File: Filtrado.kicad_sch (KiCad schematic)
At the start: 31 parts

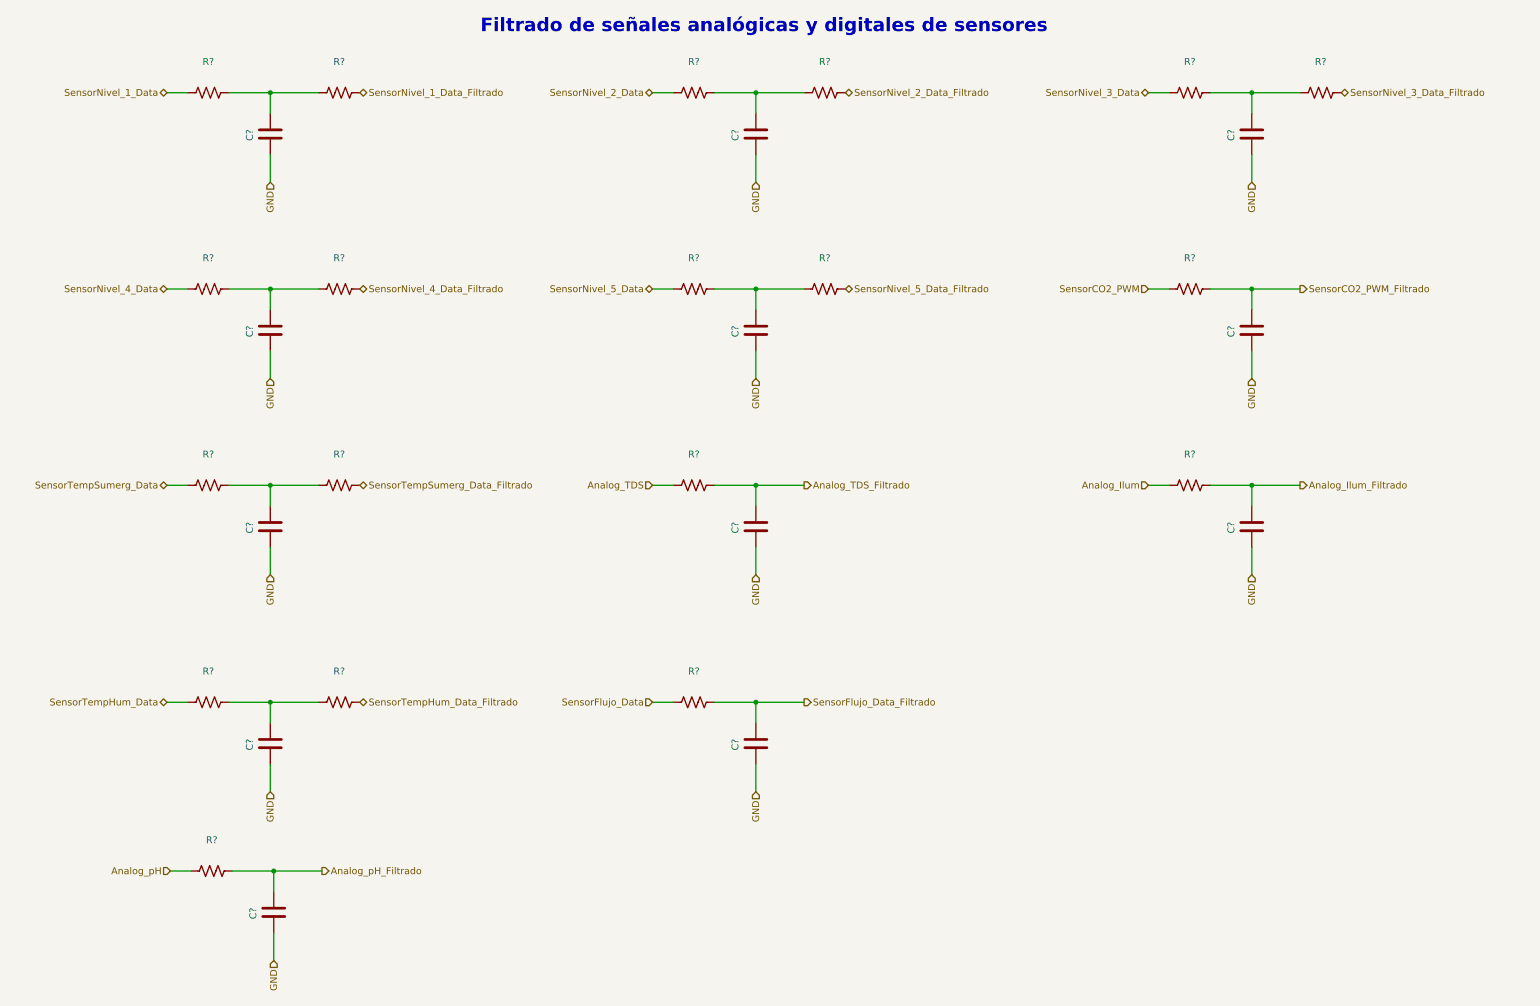
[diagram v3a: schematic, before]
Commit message: Actualización de SCH según placa industrial, y búsqueda de footprints.
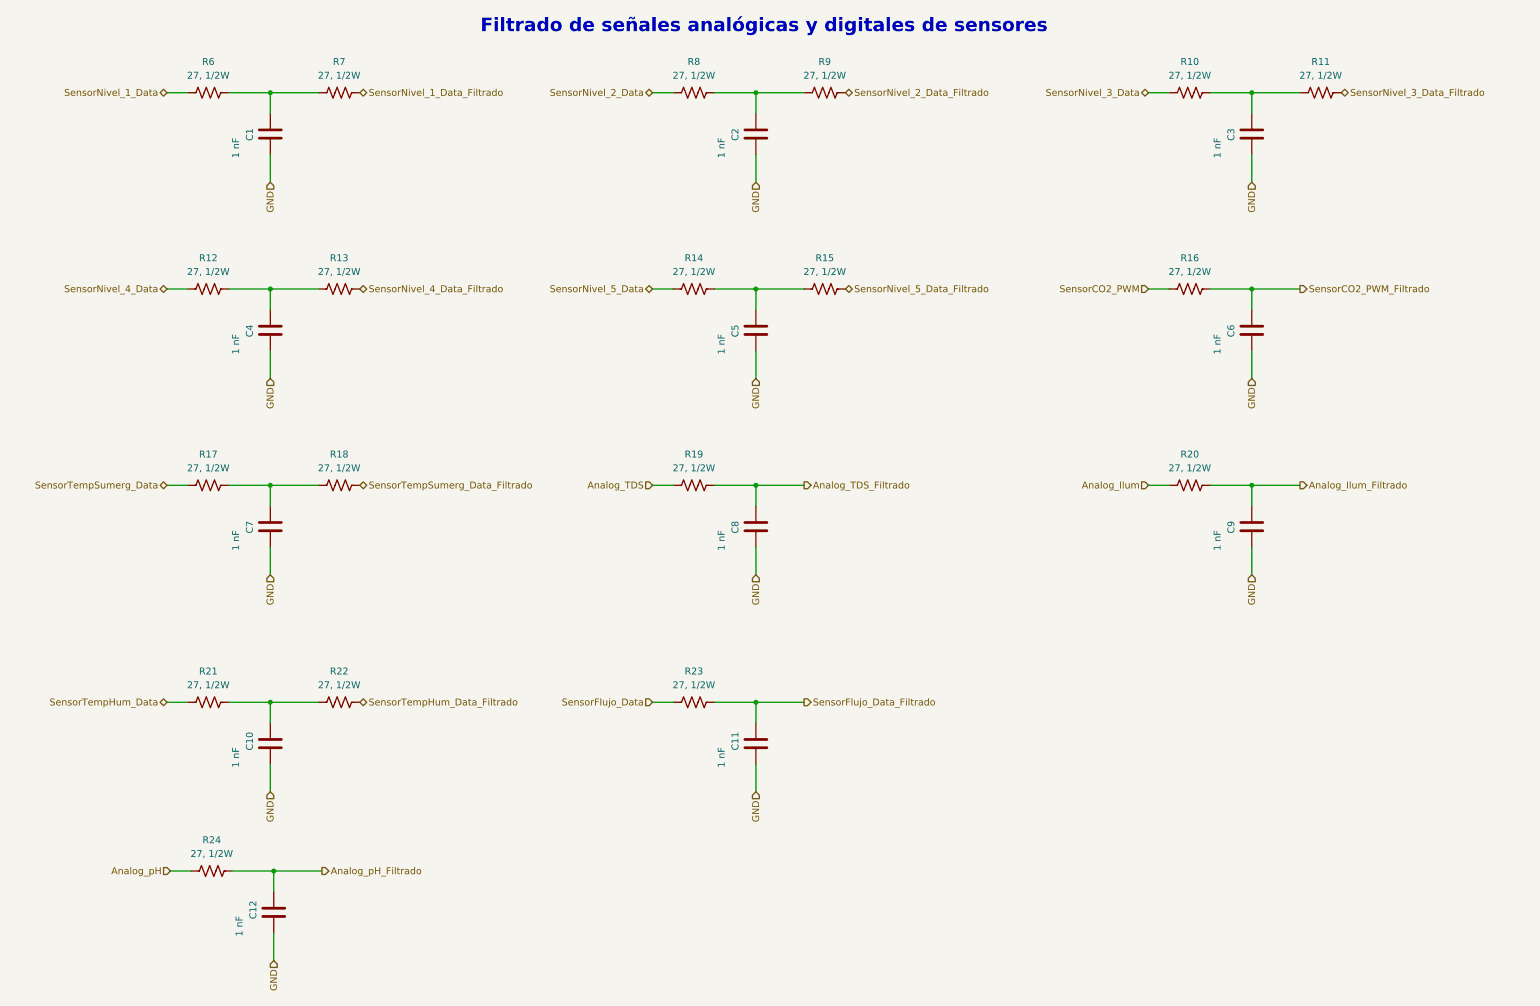
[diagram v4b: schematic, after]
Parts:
- C1, C10, C11, C12, C2, C3, C4, C5, C6, C7, C8, C9: renamed from C?; value (none) -> 1 nF
- R10, R11, R12, R13, R14, R15, R16, R17, R18, R19, R20, R21, R22, R23, R24, R6, R7, R8, R9: renamed from R?; value (none) -> 27, 1/2W

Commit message: Fin de SCH, config de inicio para PCB
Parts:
- C1, C10, C11, C12, C2, C3, C4, C5, C6, C7, C8, C9: footprint (none) -> Capacitor_SMD:C_0805_2012Metric
- R10, R11, R12, R13, R14, R15, R16, R17, R18, R19, R20, R21, R22, R23, R24, R6, R7, R8, R9: footprint (none) -> Resistor_SMD:R_0805_2012Metric
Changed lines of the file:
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@@
     (property "Reference" "R15" (id 0) (at 160.02 59.055 90))
     (property "Value" "27, 1/2W" (id 1) (at 160.02 61.595 90))
-    (property "Footprint" "" (id 2) (at 160.274 63.754 90)
+    (property "Footprint" "Resistor_SMD:R_0805_2012Metric" (id 2) (at 160.274 63.754 90)
       (effects (font (size 1.27 1.27)) hide)
     )
@@
       (effects (font (size 1.27 1.27)) (justify left))
     )
-    (property "Footprint" "" (id 2) (at 148.2852 152.4 0)
+    (property "Footprint" "Capacitor_SMD:C_0805_2012Metric" (id 2) (at 148.2852 152.4 0)
       (effects (font (size 1.27 1.27)) hide)
     )
@@
     (property "Reference" "R7" (id 0) (at 70.485 22.86 90))
     (property "Value" "27, 1/2W" (id 1) (at 70.485 25.4 90))
-    (property "Footprint" "" (id 2) (at 70.739 27.559 90)
+    (property "Footprint" "Resistor_SMD:R_0805_2012Metric" (id 2) (at 70.739 27.559 90)
       (effects (font (size 1.27 1.27)) hide)
     )
@@
       (effects (font (size 1.27 1.27)) (justify left))
     )
-    (property "Footprint" "" (id 2) (at 59.3852 183.515 0)
+    (property "Footprint" "Capacitor_SMD:C_0805_2012Metric" (id 2) (at 59.3852 183.515 0)
       (effects (font (size 1.27 1.27)) hide)
     )
@@
     (property "Reference" "R16" (id 0) (at 227.33 59.055 90))
     (property "Value" "27, 1/2W" (id 1) (at 227.33 61.595 90))
-    (property "Footprint" "" (id 2) (at 227.584 63.754 90)
+    (property "Footprint" "Resistor_SMD:R_0805_2012Metric" (id 2) (at 227.584 63.754 90)
       (effects (font (size 1.27 1.27)) hide)
     )
@@
     (property "Reference" "R24" (id 0) (at 46.99 166.37 90))
     (property "Value" "27, 1/2W" (id 1) (at 46.99 168.91 90))
-    (property "Footprint" "" (id 2) (at 47.244 171.069 90)
+    (property "Footprint" "Resistor_SMD:R_0805_2012Metric" (id 2) (at 47.244 171.069 90)
       (effects (font (size 1.27 1.27)) hide)
     )
@@
     (property "Reference" "R14" (id 0) (at 135.89 59.055 90))
     (property "Value" "27, 1/2W" (id 1) (at 135.89 61.595 90))
-    (property "Footprint" "" (id 2) (at 136.144 63.754 90)
+    (property "Footprint" "Resistor_SMD:R_0805_2012Metric" (id 2) (at 136.144 63.754 90)
       (effects (font (size 1.27 1.27)) hide)
     )
@@
       (effects (font (size 1.27 1.27)) (justify left))
     )
-    (property "Footprint" "" (id 2) (at 58.7502 40.005 0)
+    (property "Footprint" "Capacitor_SMD:C_0805_2012Metric" (id 2) (at 58.7502 40.005 0)
       (effects (font (size 1.27 1.27)) hide)
     )
@@
       (effects (font (size 1.27 1.27)) (justify left))
     )
-    (property "Footprint" "" (id 2) (at 58.7502 112.395 0)
+    (property "Footprint" "Capacitor_SMD:C_0805_2012Metric" (id 2) (at 58.7502 112.395 0)
       (effects (font (size 1.27 1.27)) hide)
     )
@@
     (property "Reference" "R9" (id 0) (at 160.02 22.86 90))
     (property "Value" "27, 1/2W" (id 1) (at 160.02 25.4 90))
-    (property "Footprint" "" (id 2) (at 160.274 27.559 90)
+    (property "Footprint" "Resistor_SMD:R_0805_2012Metric" (id 2) (at 160.274 27.559 90)
       (effects (font (size 1.27 1.27)) hide)
     )
@@
       (effects (font (size 1.27 1.27)) (justify left))
     )
-    (property "Footprint" "" (id 2) (at 58.7502 76.2 0)
+    (property "Footprint" "Capacitor_SMD:C_0805_2012Metric" (id 2) (at 58.7502 76.2 0)
       (effects (font (size 1.27 1.27)) hide)
     )
@@
       (effects (font (size 1.27 1.27)) (justify left))
     )
-    (property "Footprint" "" (id 2) (at 148.2852 40.005 0)
+    (property "Footprint" "Capacitor_SMD:C_0805_2012Metric" (id 2) (at 148.2852 40.005 0)
       (effects (font (size 1.27 1.27)) hide)
     )
@@
       (effects (font (size 1.27 1.27)) (justify left))
     )
-    (property "Footprint" "" (id 2) (at 239.7252 40.005 0)
+    (property "Footprint" "Capacitor_SMD:C_0805_2012Metric" (id 2) (at 239.7252 40.005 0)
       (effects (font (size 1.27 1.27)) hide)
     )
@@
     (property "Reference" "R22" (id 0) (at 70.485 135.255 90))
     (property "Value" "27, 1/2W" (id 1) (at 70.485 137.795 90))
-    (property "Footprint" "" (id 2) (at 70.739 139.954 90)
+    (property "Footprint" "Resistor_SMD:R_0805_2012Metric" (id 2) (at 70.739 139.954 90)
       (effects (font (size 1.27 1.27)) hide)
     )
@@
     (property "Reference" "R19" (id 0) (at 135.89 95.25 90))
     (property "Value" "27, 1/2W" (id 1) (at 135.89 97.79 90))
-    (property "Footprint" "" (id 2) (at 136.144 99.949 90)
+    (property "Footprint" "Resistor_SMD:R_0805_2012Metric" (id 2) (at 136.144 99.949 90)
       (effects (font (size 1.27 1.27)) hide)
     )
@@
     (property "Reference" "R21" (id 0) (at 46.355 135.255 90))
     (property "Value" "27, 1/2W" (id 1) (at 46.355 137.795 90))
-    (property "Footprint" "" (id 2) (at 46.609 139.954 90)
+    (property "Footprint" "Resistor_SMD:R_0805_2012Metric" (id 2) (at 46.609 139.954 90)
       (effects (font (size 1.27 1.27)) hide)
     )
@@
     (property "Reference" "R13" (id 0) (at 70.485 59.055 90))
     (property "Value" "27, 1/2W" (id 1) (at 70.485 61.595 90))
-    (property "Footprint" "" (id 2) (at 70.739 63.754 90)
+    (property "Footprint" "Resistor_SMD:R_0805_2012Metric" (id 2) (at 70.739 63.754 90)
       (effects (font (size 1.27 1.27)) hide)
     )
@@
     (property "Reference" "R20" (id 0) (at 227.33 95.25 90))
     (property "Value" "27, 1/2W" (id 1) (at 227.33 97.79 90))
-    (property "Footprint" "" (id 2) (at 227.584 99.949 90)
+    (property "Footprint" "Resistor_SMD:R_0805_2012Metric" (id 2) (at 227.584 99.949 90)
       (effects (font (size 1.27 1.27)) hide)
     )
@@
       (effects (font (size 1.27 1.27)) (justify left))
     )
-    (property "Footprint" "" (id 2) (at 239.7252 112.395 0)
+    (property "Footprint" "Capacitor_SMD:C_0805_2012Metric" (id 2) (at 239.7252 112.395 0)
       (effects (font (size 1.27 1.27)) hide)
     )
@@
     (property "Reference" "R8" (id 0) (at 135.89 22.86 90))
     (property "Value" "27, 1/2W" (id 1) (at 135.89 25.4 90))
-    (property "Footprint" "" (id 2) (at 136.144 27.559 90)
+    (property "Footprint" "Resistor_SMD:R_0805_2012Metric" (id 2) (at 136.144 27.559 90)
       (effects (font (size 1.27 1.27)) hide)
     )
@@
     (property "Reference" "R11" (id 0) (at 251.46 22.86 90))
     (property "Value" "27, 1/2W" (id 1) (at 251.46 25.4 90))
-    (property "Footprint" "" (id 2) (at 251.714 27.559 90)
+    (property "Footprint" "Resistor_SMD:R_0805_2012Metric" (id 2) (at 251.714 27.559 90)
       (effects (font (size 1.27 1.27)) hide)
     )
@@
       (effects (font (size 1.27 1.27)) (justify left))
     )
-    (property "Footprint" "" (id 2) (at 58.7502 152.4 0)
+    (property "Footprint" "Capacitor_SMD:C_0805_2012Metric" (id 2) (at 58.7502 152.4 0)
       (effects (font (size 1.27 1.27)) hide)
     )
@@
     (property "Reference" "R23" (id 0) (at 135.89 135.255 90))
     (property "Value" "27, 1/2W" (id 1) (at 135.89 137.795 90))
-    (property "Footprint" "" (id 2) (at 136.144 139.954 90)
+    (property "Footprint" "Resistor_SMD:R_0805_2012Metric" (id 2) (at 136.144 139.954 90)
       (effects (font (size 1.27 1.27)) hide)
     )
@@
     (property "Reference" "R18" (id 0) (at 70.485 95.25 90))
     (property "Value" "27, 1/2W" (id 1) (at 70.485 97.79 90))
-    (property "Footprint" "" (id 2) (at 70.739 99.949 90)
+    (property "Footprint" "Resistor_SMD:R_0805_2012Metric" (id 2) (at 70.739 99.949 90)
       (effects (font (size 1.27 1.27)) hide)
     )
@@
     (property "Reference" "R17" (id 0) (at 46.355 95.25 90))
     (property "Value" "27, 1/2W" (id 1) (at 46.355 97.79 90))
-    (property "Footprint" "" (id 2) (at 46.609 99.949 90)
+    (property "Footprint" "Resistor_SMD:R_0805_2012Metric" (id 2) (at 46.609 99.949 90)
       (effects (font (size 1.27 1.27)) hide)
     )
@@
     (property "Reference" "R10" (id 0) (at 227.33 22.86 90))
     (property "Value" "27, 1/2W" (id 1) (at 227.33 25.4 90))
-    (property "Footprint" "" (id 2) (at 227.584 27.559 90)
+    (property "Footprint" "Resistor_SMD:R_0805_2012Metric" (id 2) (at 227.584 27.559 90)
       (effects (font (size 1.27 1.27)) hide)
     )
@@
       (effects (font (size 1.27 1.27)) (justify left))
     )
-    (property "Footprint" "" (id 2) (at 148.2852 76.2 0)
+    (property "Footprint" "Capacitor_SMD:C_0805_2012Metric" (id 2) (at 148.2852 76.2 0)
       (effects (font (size 1.27 1.27)) hide)
     )
@@
       (effects (font (size 1.27 1.27)) (justify left))
     )
-    (property "Footprint" "" (id 2) (at 239.7252 76.2 0)
+    (property "Footprint" "Capacitor_SMD:C_0805_2012Metric" (id 2) (at 239.7252 76.2 0)
       (effects (font (size 1.27 1.27)) hide)
     )
@@
     (property "Reference" "R12" (id 0) (at 46.355 59.055 90))
     (property "Value" "27, 1/2W" (id 1) (at 46.355 61.595 90))
-    (property "Footprint" "" (id 2) (at 46.609 63.754 90)
+    (property "Footprint" "Resistor_SMD:R_0805_2012Metric" (id 2) (at 46.609 63.754 90)
       (effects (font (size 1.27 1.27)) hide)
     )
@@
     (property "Reference" "R6" (id 0) (at 46.355 22.86 90))
     (property "Value" "27, 1/2W" (id 1) (at 46.355 25.4 90))
-    (property "Footprint" "" (id 2) (at 46.609 27.559 90)
+    (property "Footprint" "Resistor_SMD:R_0805_2012Metric" (id 2) (at 46.609 27.559 90)
       (effects (font (size 1.27 1.27)) hide)
     )
@@
       (effects (font (size 1.27 1.27)) (justify left))
     )
-    (property "Footprint" "" (id 2) (at 148.2852 112.395 0)
-      (effects (font (size 1.27 1.27)) hide)
-    )
+    (property "Footprint" "Capacitor_SMD:C_0805_2012Metric" (id 2) (at 148.2852 112.395 0)
+      (effects (font (size 1.27 1.27)) hide)
+    )
